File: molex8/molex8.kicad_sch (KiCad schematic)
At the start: 7 parts, among them J1 Conn_01x04, J2 Conn_02x04_Counter_Clockwise, J3 Conn_01x04

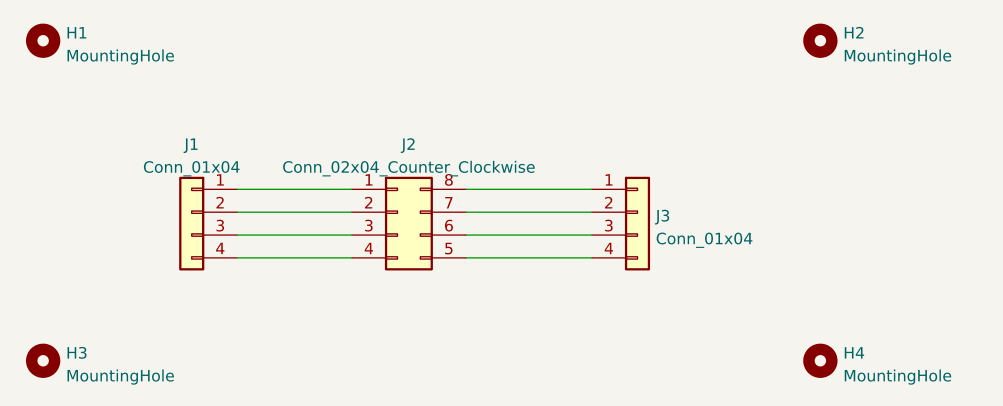
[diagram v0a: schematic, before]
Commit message: Use screw terminal symbols, use MVE25-5-V as values.
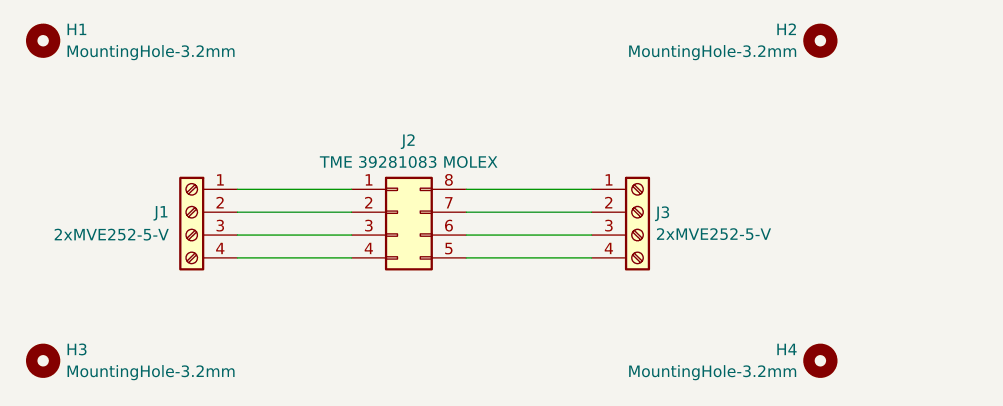
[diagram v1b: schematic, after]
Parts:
- H1, H2, H3, H4: value MountingHole -> MountingHole-3.2mm
- J1, J3: value Conn_01x04 -> 2xMVE252-5-V; symbol Connector_Generic:Conn_01x04 -> Connector:Screw_Terminal_01x04
- J2: value Conn_02x04_Counter_Clockwise -> TME 39281083 MOLEX
